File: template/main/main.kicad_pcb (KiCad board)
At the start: 2 copper layers, 99.1 x 99.1 mm, 7 parts, among them J2 PinHeader_01x05_P2.54_THT_ang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

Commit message: PM-RQ8
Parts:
- added PE1: PE, kicad_inventree_lib:PE, F.Cu at (43.2, 146.1)
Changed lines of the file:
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@@
 	(net 10 "+5V_BUS")
 	(net 11 "/SCL")
+	(net 12 "unconnected-(PE1-Pad1)")
 	(footprint "kicad_inventree_lib:PM-front-02x04"
 		(layer "F.Cu")
@@
 		)
 	)
+	(footprint "kicad_inventree_lib:PE"
+		(layer "F.Cu")
+		(at 43.18 146.05)
+		(property "Reference" "PE1"
+			(at 0 -6.5 0)
+			(unlocked yes)
+			(layer "F.SilkS")
+			(hide yes)
+			(effects
+				(font
+					(size 1 1)
+					(thickness 0.1)
+				)
+			)
+		)
+		(property "Value" "PE"
+			(at 0 -5 0)
+			(unlocked yes)
+			(layer "F.Fab")
+			(effects
+				(font
+					(size 1 1)
+					(thickness 0.15)
+				)
+			)
+		)
+		(property "Footprint" "kicad_inventree_lib:PE"
+			(at 0 -6 0)
+			(unlocked yes)
+			(layer "F.Fab")
+			(hide yes)
+			(effects
+				(font
+					(size 1 1)
+					(thickness 0.15)
+				)
+			)
+		)
+		(property "Datasheet" ""
+			(at 0 -6 0)
+			(unlocked yes)
+			(layer "F.Fab")
+			(hide yes)
+			(effects
+				(font
+					(size 1 1)
+					(thickness 0.15)
+				)
+			)
+		)
+		(property "Description" "Power symbol creates a global label with name \"Earth_Protective\""
+			(at 0 -6 0)
+			(unlocked yes)
+			(layer "F.Fab")
+			(hide yes)
+			(effects
+				(font
+					(size 1 1)
+					(thickness 0.15)
+				)
+			)
+		)
+		(sheetname "Корневой лист")
+		(sheetfile "main.kicad_sch")
+		(attr smd exclude_from_bom)
+		(fp_text user "${REFERENCE}"
+			(at 0 -3.5 0)
+			(unlocked yes)
+			(layer "F.Fab")
+			(effects
+				(font
+					(size 1 1)
+					(thickness 0.15)
+				)
+			)
+		)
+		(pad "1" thru_hole oval
+			(at 0 0)
+			(size 6.35 6.35)
+			(drill 3.2)
+			(layers "*.Cu" "*.Mask")
+			(remove_unused_layers no)
+			(net 12 "unconnected-(PE1-Pad1)")
+			(pintype "power_in")
+		)
+	)

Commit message: PM-ESPC3
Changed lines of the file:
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@@
 	)
 	(gr_text "SCL"
-		(at 114.3 106.045 0)
+		(at 116.84 97.79 0)
 		(layer "F.SilkS" knockout)
 		(effects
@@
 				(bold yes)
 			)
-			(justify left bottom)
 		)
 	)
-	(gr_text "+3.3V"
-		(at 113.442857 98.425 0)
+	(gr_text "SDA"
+		(at 116.84 95.25 0)
 		(layer "F.SilkS" knockout)
 		(effects
@@
 				(bold yes)
 			)
-			(justify left bottom)
 		)
 	)
 	(gr_text "GND"
-		(at 114.157143 100.965 0)
+		(at 116.84 105.41 0)
 		(layer "F.SilkS" knockout)
 		(effects
@@
 				(bold yes)
 			)
-			(justify left bottom)
-		)
-	)
-	(gr_text "+5V"
-		(at 114.157143 95.885 0)
-		(layer "F.SilkS" knockout)
-		(effects
-			(font
-				(size 1 1)
-				(thickness 0.2)
-				(bold yes)
-			)
-			(justify left bottom)
-		)
-	)
-	(gr_text "SDA"
-		(at 114.27619 103.505 0)
-		(layer "F.SilkS" knockout)
-		(effects
-			(font
-				(size 1 1)
-				(thickness 0.2)
-				(bold yes)
-			)
-			(justify left bottom)
 		)
 	)
@@
 		)
 	)
+	(gr_text "+5V"
+		(at 116.84 100.33 0)
+		(layer "F.SilkS" knockout)
+		(effects
+			(font
+				(size 1 1)
+				(thickness 0.2)
+				(bold yes)
+			)
+		)
+	)
+	(gr_text "+3.3V"
+		(at 116.84 102.87 0)
+		(layer "F.SilkS" knockout)
+		(effects
+			(font
+				(size 1 1)
+				(thickness 0.2)
+				(bold yes)
+			)
+		)
+	)

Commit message: PM-DI16
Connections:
- J2 pad 1: +5V_BUS -> /SDA
- J2 pad 2: +3.3V_BUS -> /SCL
- J2 pad 3: GND -> +5V
- J2 pad 4: /SDA -> +3.3V
- J2 pad 5: /SCL -> GND
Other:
- board text added: "CS"
- board text added: "MISO"
- board text added: "MOSI"
- board text added: "PE"
- board text added: "SCK"
- board text added: "V0+"
- board text added: "V0-"
- board text added: "V1+"
- board text added: "V1-"
- board text added: "V2+"
- board text added: "V2-"
- board text added: "V3+"
- board text added: "V3-"
- board text added: "V4+"
- board text added: "V4-"
- board text added: "V5+"
- board text added: "V5-"
- board text added: "V6+"
- board text added: "V6-"
- board text added: "V7+"
- board text added: "V7-"

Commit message: PM-RQ8
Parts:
- moved oshw_logo 59.7 mm to (120.7, 138.4)
- moved kicad_logo 59.7 mm to (120.7, 125.7)
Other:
- outline, holes or cut-outs redrawn
- board text added: "1"
- board text added: "10+"
- board text added: "2"
- board text added: "4"
- board text added: "OFF"
- board text added: "ON"
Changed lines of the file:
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@@
 	(footprint "Symbol:KiCad-Logo2_5mm_SilkScreen"
 		(layer "B.Cu")
-		(at 119.38 66.04 90)
+		(at 120.65 125.73 90)
 		(descr "KiCad Logo")
 		(tags "Logo KiCad")
@@
 	(footprint "Symbol:OSHW-Symbol_6.7x6mm_SilkScreen"
 		(layer "B.Cu")
-		(at 119.38 78.74 90)
+		(at 120.65 138.43 90)
 		(descr "Open Source Hardware Symbol")
 		(tags "Logo Symbol OSHW")
@@
 	)
 	(gr_line
+		(start 99.06 52.07)
+		(end 99.06 66.04)
+		(stroke
+			(width 0.1)
+			(type default)
+		)
+		(layer "F.SilkS")
+	)
+	(gr_line
+		(start 99.06 66.04)
+		(end 116.84 66.04)
+		(stroke
+			(width 0.1)
+			(type default)
+		)
+		(layer "F.SilkS")
+	)
+	(gr_line
+		(start 116.84 66.04)
+		(end 116.84 62.23)
+		(stroke
+			(width 0.1)
+			(type default)
+		)
+		(layer "F.SilkS")
+	)
+	(gr_line
 		(start 24.13 101.6)
 		(end 13.97 101.6)
@@
 		)
 		(layer "Cmts.User")
+	)
+	(gr_line
+		(start 116.84 54.61)
+		(end 116.84 60.96)
+		(stroke
+			(width 0.05)
+			(type default)
+		)
+		(layer "Edge.Cuts")
+	)
+	(gr_arc
+		(start 116.84 60.96)
+		(mid 116.468026 61.858026)
+		(end 115.57 62.23)
+		(stroke
+			(width 0.05)
+			(type default)
+		)
+		(layer "Edge.Cuts")
 	)
 	(gr_line
@@
 		(layer "Edge.Cuts")
 	)
+	(gr_arc
+		(start 105.41 62.23)
+		(mid 104.511974 61.858026)
+		(end 104.14 60.96)
+		(stroke
+			(width 0.05)
+			(type default)
+		)
+		(layer "Edge.Cuts")
+	)
 	(gr_line
 		(start 120.65 149.86)
 		(end 29.21 149.86)
+		(stroke
+			(width 0.05)
+			(type default)
+		)
+		(layer "Edge.Cuts")
+	)
+	(gr_arc
+		(start 100.33 50.8)
+		(mid 103.024077 51.915923)
+		(end 104.14 54.61)
+		(stroke
+			(width 0.05)
+			(type default)
+		)
+		(layer "Edge.Cuts")
+	)
+	(gr_line
+		(start 104.14 54.61)
+		(end 104.14 60.96)
 		(stroke
 			(width 0.05)
@@
 		(layer "Edge.Cuts")
 	)
+	(gr_line
+		(start 105.41 62.23)
+		(end 115.57 62.23)
+		(stroke
+			(width 0.05)
+			(type default)
+		)
+		(layer "Edge.Cuts")
+	)
 	(gr_arc
 		(start 124.46 146.05)
@@
 	)
 	(gr_arc
+		(start 116.84 54.61)
+		(mid 117.955923 51.915923)
+		(end 120.65 50.8)
+		(stroke
+			(width 0.05)
+			(type default)
+		)
+		(layer "Edge.Cuts")
+	)
+	(gr_arc
 		(start 29.21 149.86)
 		(mid 26.515923 148.744077)
@@
 	(gr_line
 		(start 44.45 50.8)
-		(end 120.65 50.8)
+		(end 100.33 50.8)
 		(stroke
 			(width 0.05)
@@
 	)
 	(gr_text "PE"
-		(at 38.1 146.05 -0)
-		(layer "B.SilkS" knockout)
-		(effects
-			(font
-				(size 1 1)
-				(thickness 0.2)
-				(bold yes)
-			)
-			(justify mirror)
+		(at 48.26 146.05 -0)
+		(layer "B.SilkS" knockout)
+		(effects
+			(font
+				(size 1 1)
+				(thickness 0.2)
+				(bold yes)
+			)
+			(justify mirror)
+		)
+	)
+	(gr_text "1"
+		(at 101.6 58.42 0)
+		(layer "F.SilkS" knockout)
+		(effects
+			(font
+				(size 1 1)
+				(thickness 0.2)
+				(bold yes)
+			)
 		)
 	)
@@
 		)
 	)
+	(gr_text "10+"
+		(at 101.6 63.5 0)
+		(layer "F.SilkS" knockout)
+		(effects
+			(font
+				(size 1 1)
+				(thickness 0.2)
+				(bold yes)
+			)
+		)
+	)
 	(gr_text "SDA"
 		(at 116.84 95.25 0)
@@
 	)
 	(gr_text "PE"
-		(at 38.1 146.05 0)
+		(at 48.26 146.05 0)
+		(layer "F.SilkS" knockout)
+		(effects
+			(font
+				(size 1 1)
+				(thickness 0.2)
+				(bold yes)
+			)
+		)
+	)
+	(gr_text "ON"
+		(at 114.3 63.5 0)
 		(layer "F.SilkS" knockout)
 		(effects
@@
 		)
 	)
+	(gr_text "2"
+		(at 101.6 55.88 0)
+		(layer "F.SilkS" knockout)
+		(effects
+			(font
+				(size 1 1)
+				(thickness 0.2)
+				(bold yes)
+			)
+		)
+	)
 	(gr_text "PM-DI16-DC24sink v0.0.1"
-		(at 123.19 57.15 90)
-		(layer "F.SilkS" knockout)
-		(effects
-			(font
-				(size 1 1)
-				(thickness 0.2)
-				(bold yes)
-			)
-			(justify right bottom)
+		(at 121.92 132.08 90)
+		(layer "F.SilkS" knockout)
+		(effects
+			(font
+				(size 1 1)
+				(thickness 0.2)
+				(bold yes)
+			)
 		)
 	)
@@
 		(layer "F.SilkS" knockout)
 		(effects
+			(font
+				(size 1 1)
+				(thickness 0.2)
+				(bold yes)
+			)
+		)
+	)
+	(gr_text "4"
+		(at 101.6 53.34 0)
+		(layer "F.SilkS" knockout)
+		(effects
+			(font
+				(size 1 1)
+				(thickness 0.2)
+				(bold yes)
+			)
+		)
+	)
+	(gr_text "OFF"
+		(at 106.68 63.5 0)
+		(layer "F.SilkS" knockout)
+		(effects

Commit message: PM-PS
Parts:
- moved PE1 1.27 mm to (44.5, 146.1)
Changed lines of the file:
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@@
 	(footprint "kicad_inventree_lib:PE"
 		(layer "F.Cu")
-		(at 43.18 146.05)
+		(at 44.45 146.05)
 		(property "Reference" "PE1"
 			(at 0 -6.5 0)
@@
 	)
 	(gr_text "PE"
-		(at 48.26 146.05 -0)
+		(at 49.53 146.05 -0)
 		(layer "B.SilkS" knockout)
 		(effects
@@
 	)
 	(gr_text "PE"
-		(at 48.26 146.05 0)
+		(at 49.53 146.05 0)
 		(layer "F.SilkS" knockout)
 		(effects
@@
 	)
 	(gr_text "PM-DI16-DC24sink v0.0.1"
-		(at 121.92 132.08 90)
+		(at 123.19 142.24 90)
 		(layer "F.SilkS" knockout)
 		(effects
@@
 				(bold yes)
 			)
-		)
-	)
+			(justify left)
+		)
+	)

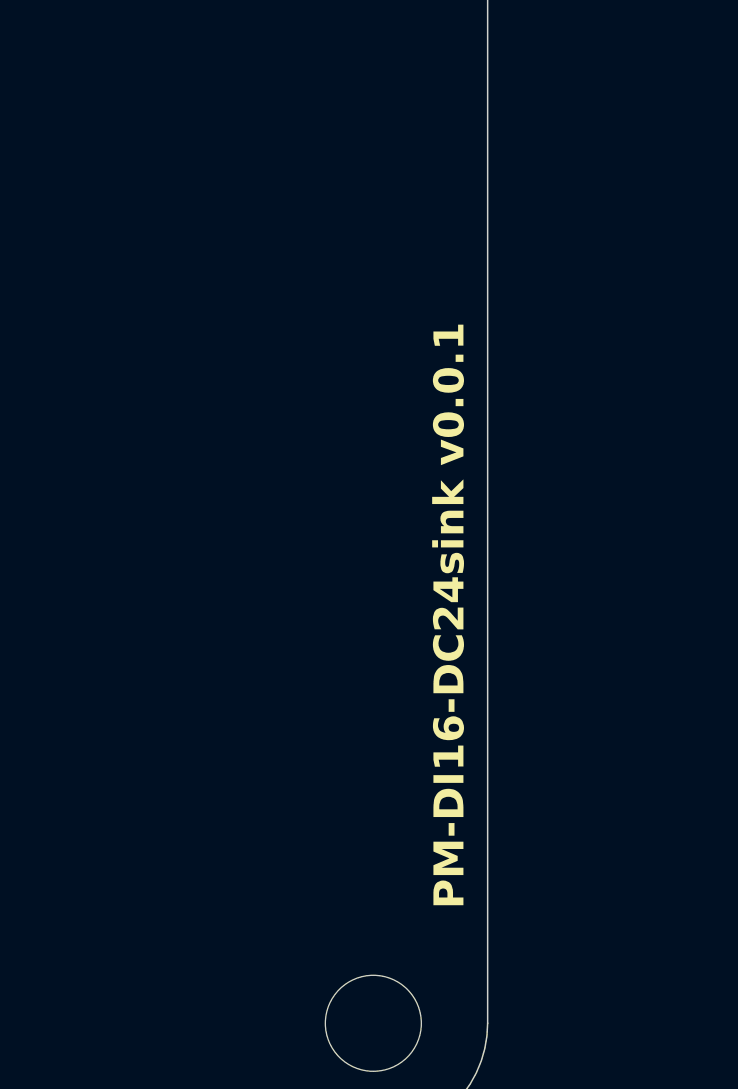
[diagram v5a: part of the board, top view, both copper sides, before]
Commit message: add version numbers
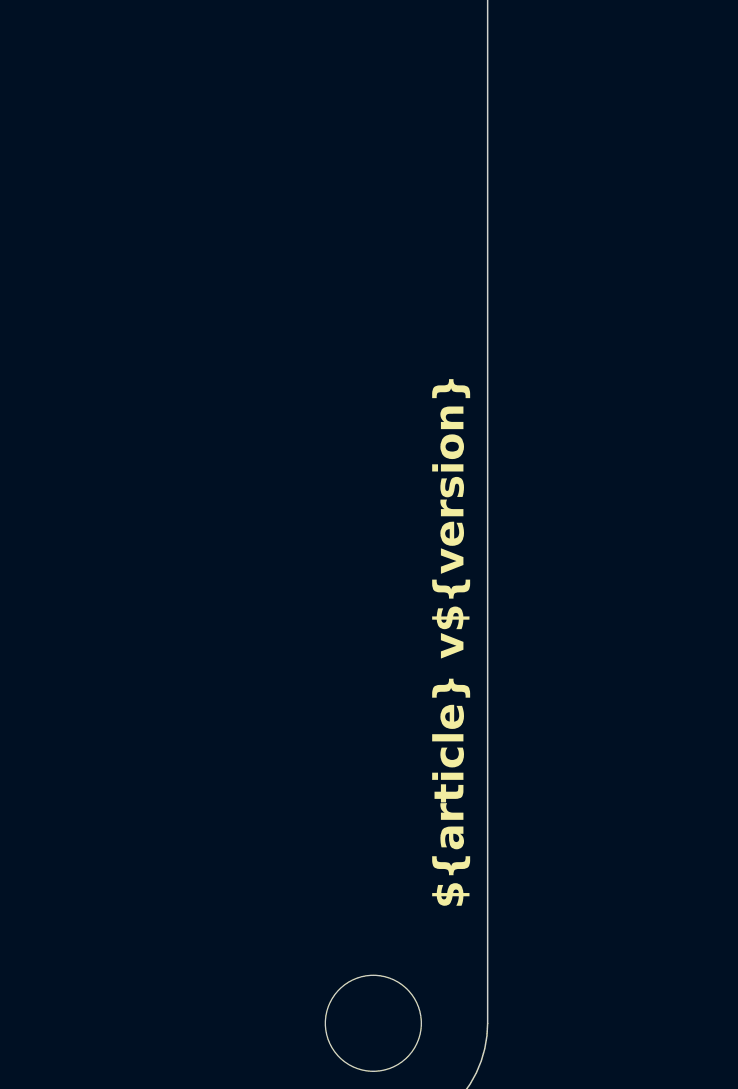
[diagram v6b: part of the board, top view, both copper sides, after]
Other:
- board text added: "${article} v${version}"
- board text removed: "PM-DI16-DC24sink v0.0.1"
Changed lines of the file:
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@@
 	)
 	(paper "A5" portrait)
+	(title_block
+		(title "${article} v${version}")
+	)
 	(layers
 		(0 "F.Cu" signal)
@@
 		)
 	)
+	(property "article" "ARTICLE")
+	(property "version" "VERSION")
 	(net 0 "")
 	(net 1 "unconnected-(J1-Pad3)")
@@
 		)
 	)
-	(gr_text "PM-DI16-DC24sink v0.0.1"
+	(gr_text "${article} v${version}"
 		(at 123.19 142.24 90)
 		(layer "F.SilkS" knockout)
